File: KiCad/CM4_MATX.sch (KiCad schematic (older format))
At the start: 9 parts

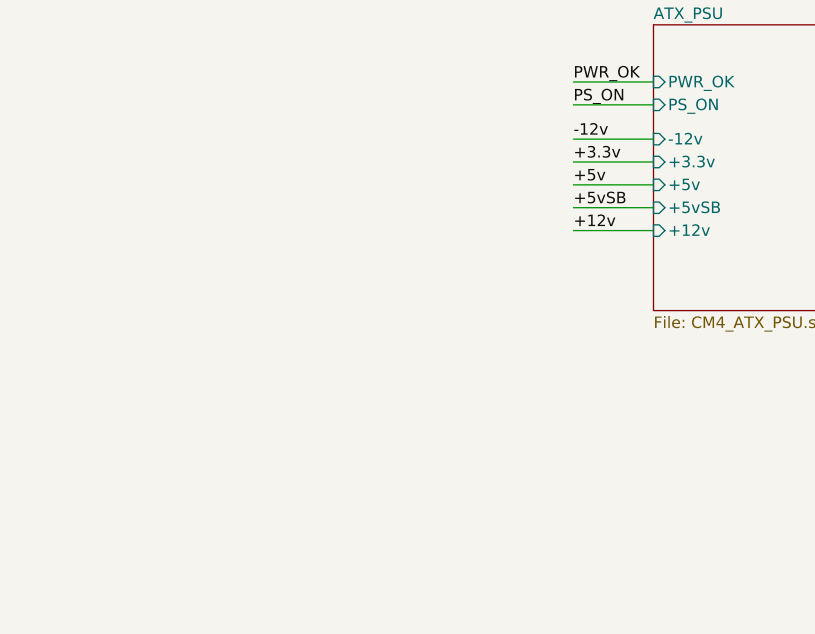
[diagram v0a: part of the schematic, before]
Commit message: Updating PCIe symbols + PCIe power stub sheet
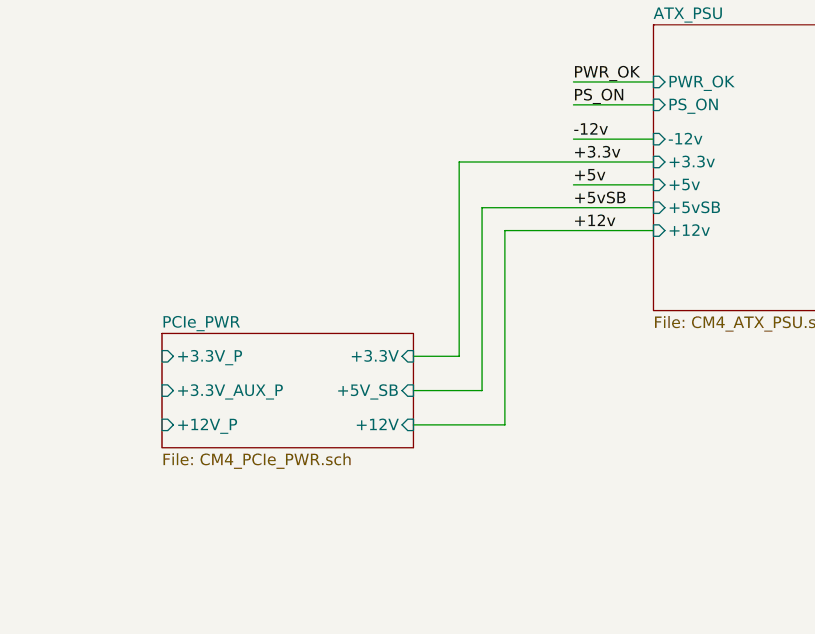
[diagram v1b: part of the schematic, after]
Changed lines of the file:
@@
 $Descr A4 11693 8268
 encoding utf-8
-Sheet 1 10
+Sheet 1 11
 Title "CM4 MATX Root Sheet"
 Date "2020-12-14"
@@
 +12v
 Wire Wire Line
-	9650 5400 10000 5400
-Wire Wire Line
-	10000 5300 9650 5300
-Wire Wire Line
 	9650 5200 10000 5200
-Wire Wire Line
-	10000 5100 9650 5100
 Wire Wire Line
 	10000 4850 9650 4850
@@
 Wire Wire Line
 	2300 1850 3050 1850
+$Sheet
+S 7850 5850 1100 500
+U 60168781
+F0 "PCIe_PWR" 50
+F1 "CM4_PCIe_PWR.sch" 50
+F2 "+12V_P" I L 7850 6250 50
+F3 "+3.3V_P" I L 7850 5950 50
+F4 "+3.3V_AUX_P" I L 7850 6100 50
+F5 "+12V" I R 8950 6250 50
+F6 "+3.3V" I R 8950 5950 50
+F7 "+5V_SB" I R 8950 6100 50
+$EndSheet
+Wire Wire Line
+	8950 5950 9150 5950
+Wire Wire Line
+	9150 5100 10000 5100
+Wire Wire Line
+	8950 6100 9250 6100
+Wire Wire Line
+	9250 5300 10000 5300
+Wire Wire Line
+	8950 6250 9350 6250
+Wire Wire Line
+	9350 5400 10000 5400
+Wire Wire Line
+	9150 5100 9150 5950
+Wire Wire Line
+	9250 5300 9250 6100
+Wire Wire Line
+	9350 5400 9350 6250
 $EndSCHEMATC

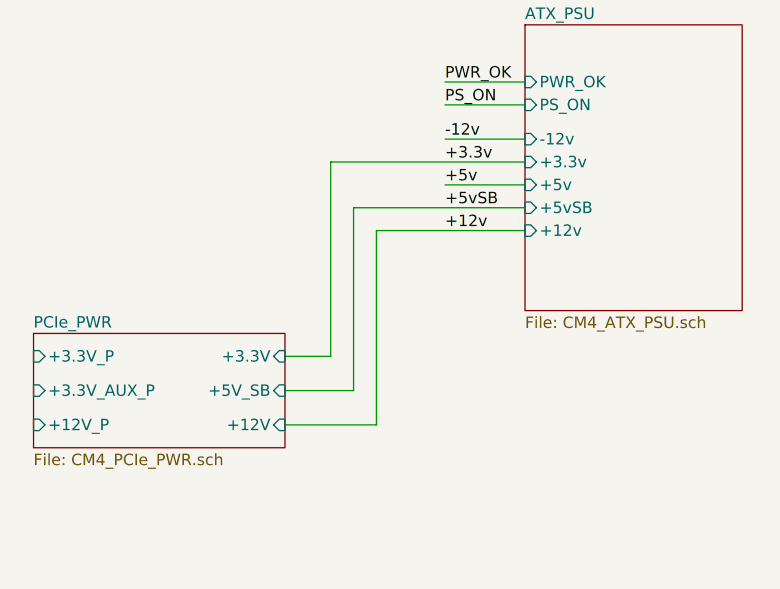
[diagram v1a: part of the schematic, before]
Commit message: Updated schematic PDF and re-did PSU-PCIe_PWR connections
Co-Authored-By: Shannon Strutz <strutz.shannon@gmail.com>
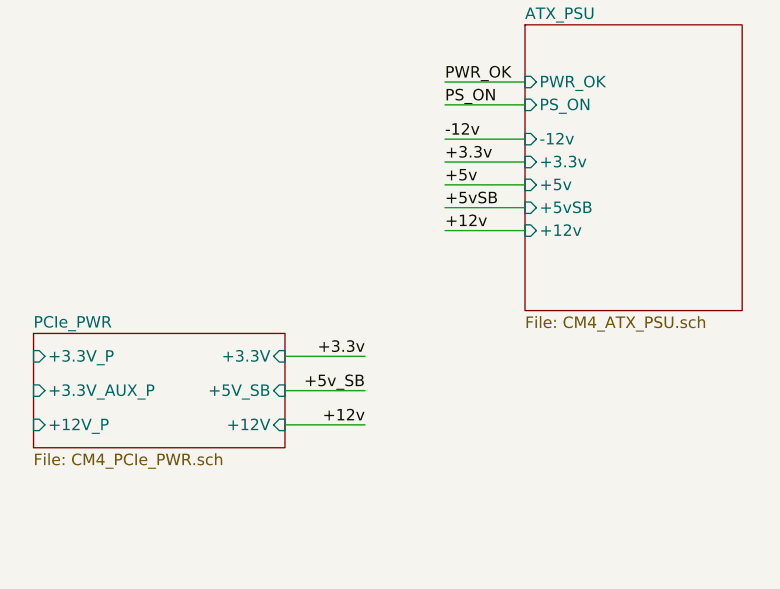
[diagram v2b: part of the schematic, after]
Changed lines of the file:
@@
 $EndSheet
 Wire Wire Line
-	8950 5950 9150 5950
+	9650 5400 10000 5400
 Wire Wire Line
-	9150 5100 10000 5100
+	10000 5100 9650 5100
 Wire Wire Line
-	8950 6100 9250 6100
+	9650 5300 10000 5300
+Text Label 9300 5950 2    50   ~ 0
++3.3v
+Text Label 9300 6100 2    50   ~ 0
++5v_SB
+Text Label 9300 6250 2    50   ~ 0
++12v
 Wire Wire Line
-	9250 5300 10000 5300
+	9300 5950 8950 5950
 Wire Wire Line
-	8950 6250 9350 6250
+	8950 6100 9300 6100
 Wire Wire Line
-	9350 5400 10000 5400
-Wire Wire Line
-	9150 5100 9150 5950
-Wire Wire Line
-	9250 5300 9250 6100
-Wire Wire Line
-	9350 5400 9350 6250
+	8950 6250 9300 6250
 $EndSCHEMATC
